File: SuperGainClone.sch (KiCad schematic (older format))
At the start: 99 parts, among them J1 Conn_01x02, J2 Conn_01x03, J3 Conn_01x02, J4 Conn_01x02, J5 Conn_01x02, Q1 TIP41C, Q2 TIP42C, U1 OPA2604A, U2 LM3886T, U3 OPA2604A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

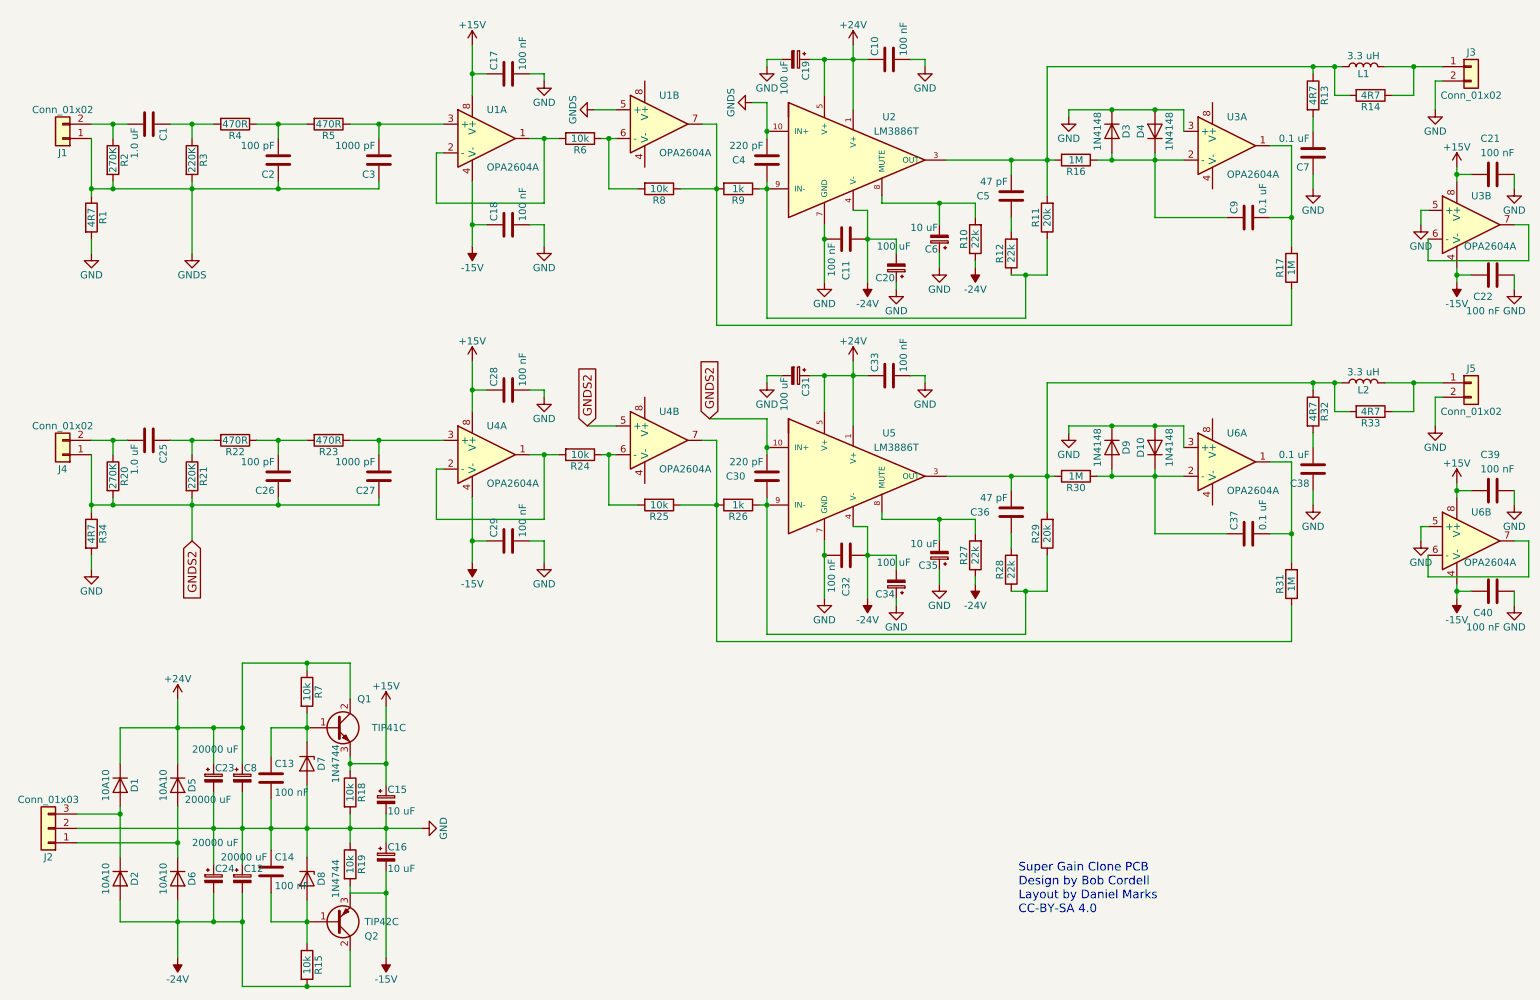
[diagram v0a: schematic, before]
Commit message: Rearranged some components
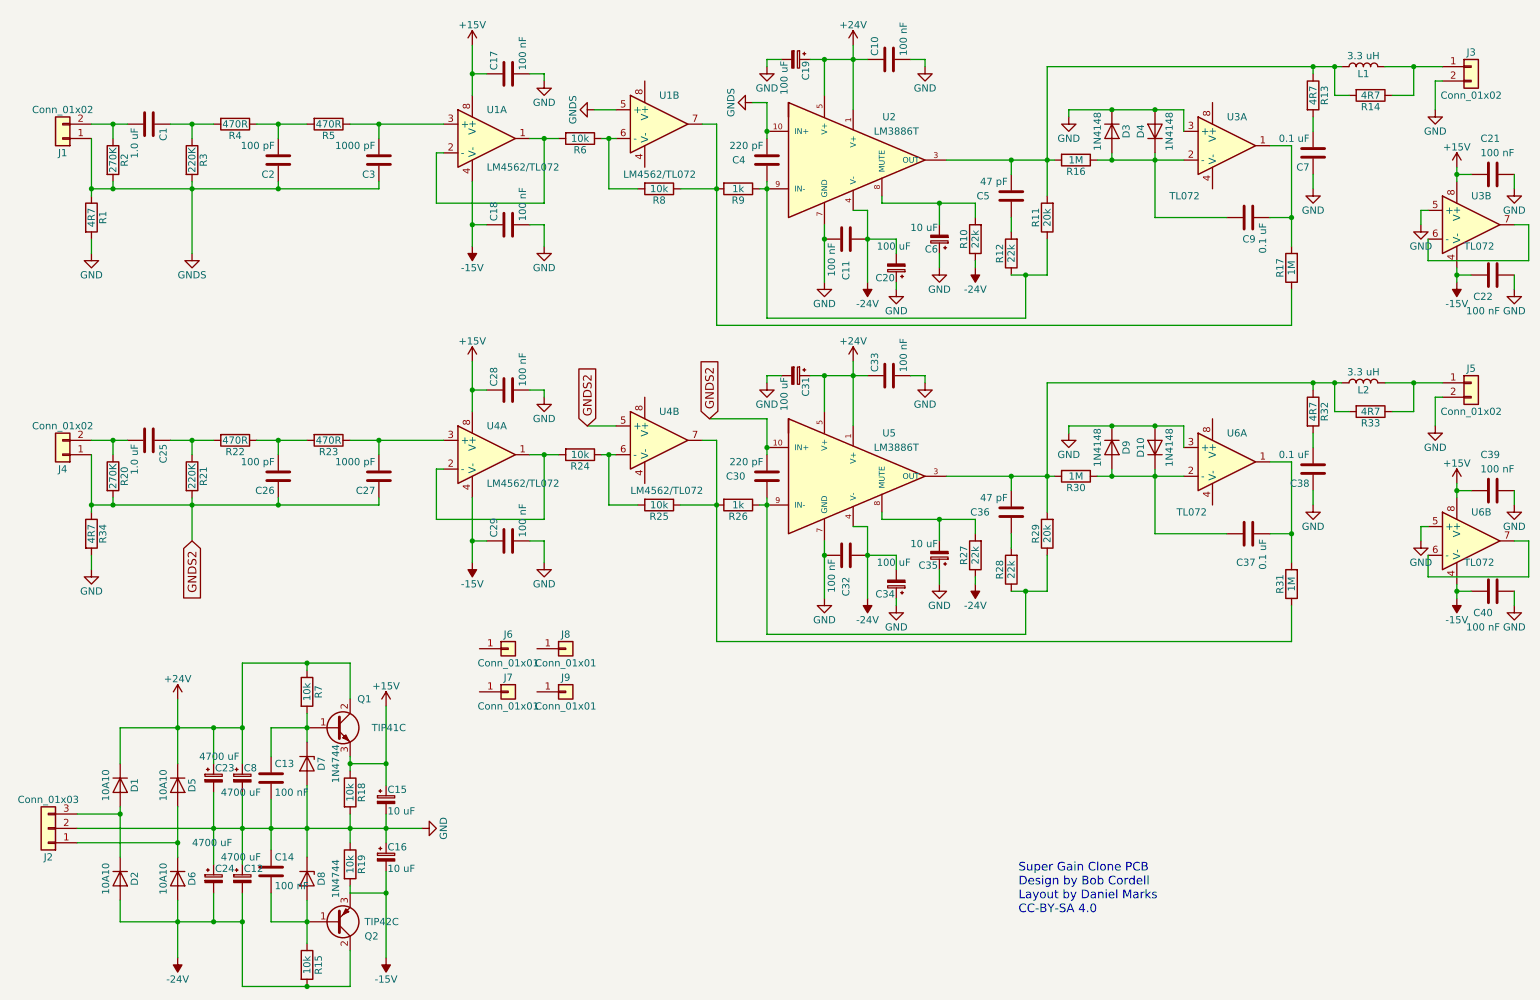
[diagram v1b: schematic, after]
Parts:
- added J6, J7, J8, J9: Conn_01x01, Connectors:1pin, symbol Conn_01x01
- C12, C23, C24, C8: value 20000 uF -> 4700 uF
- U1, U4: value OPA2604A -> LM4562/TL072
- U3, U6: value OPA2604A -> TL072

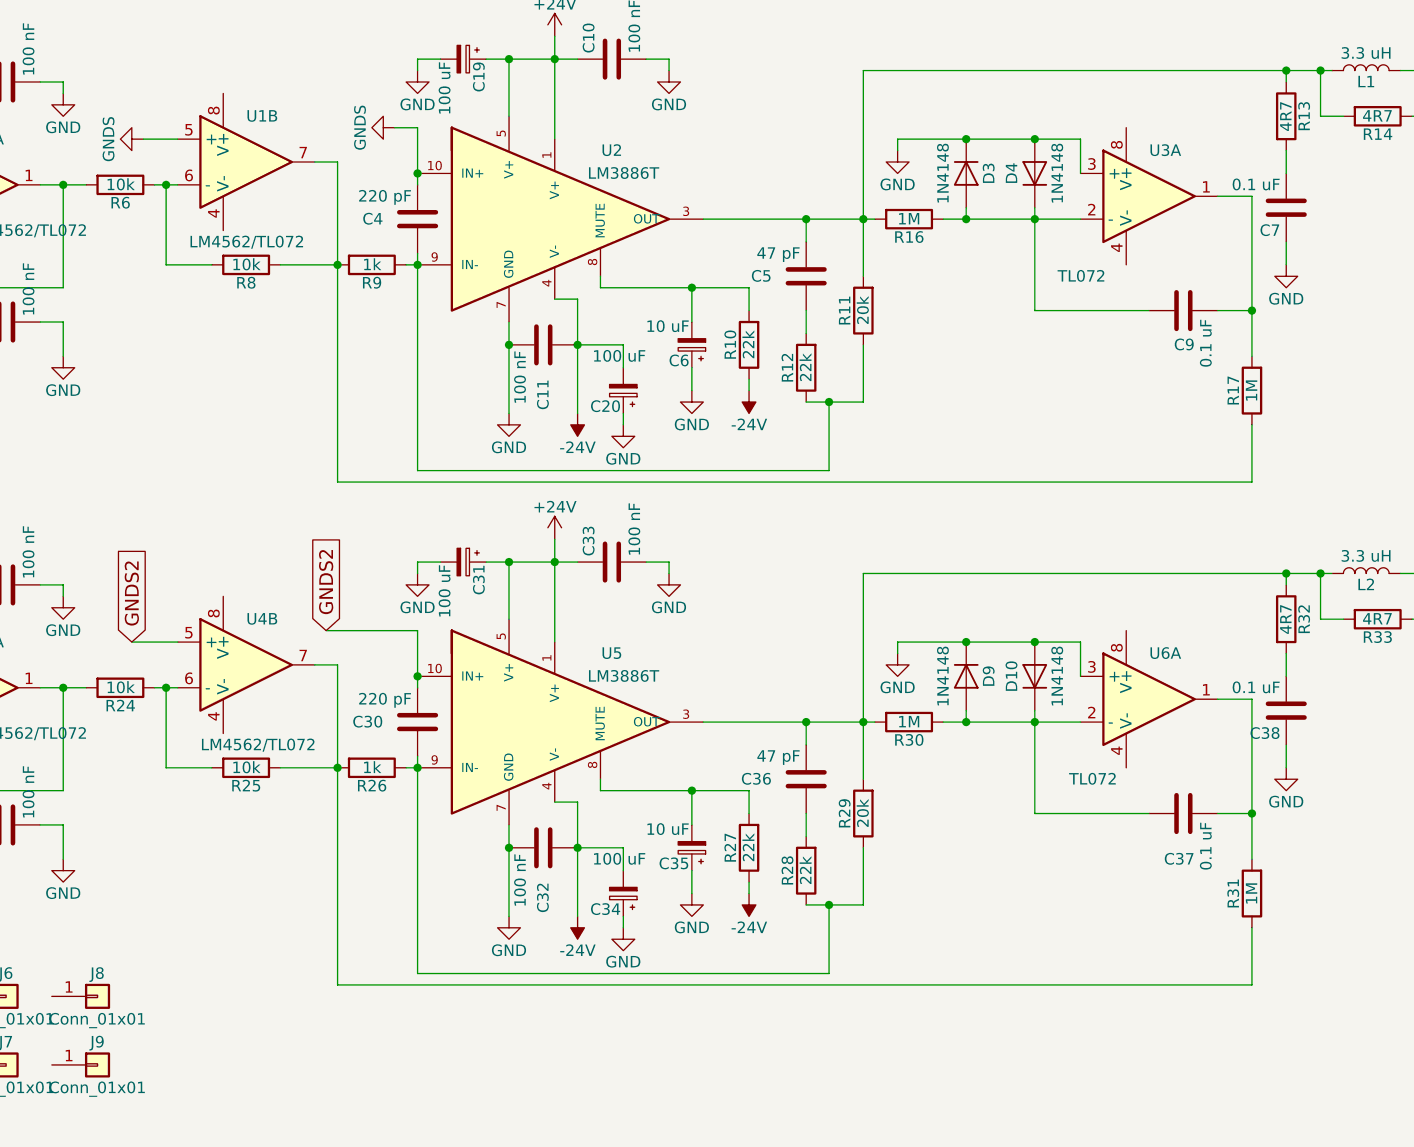
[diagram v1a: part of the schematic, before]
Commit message: Fixed DC servo feedback
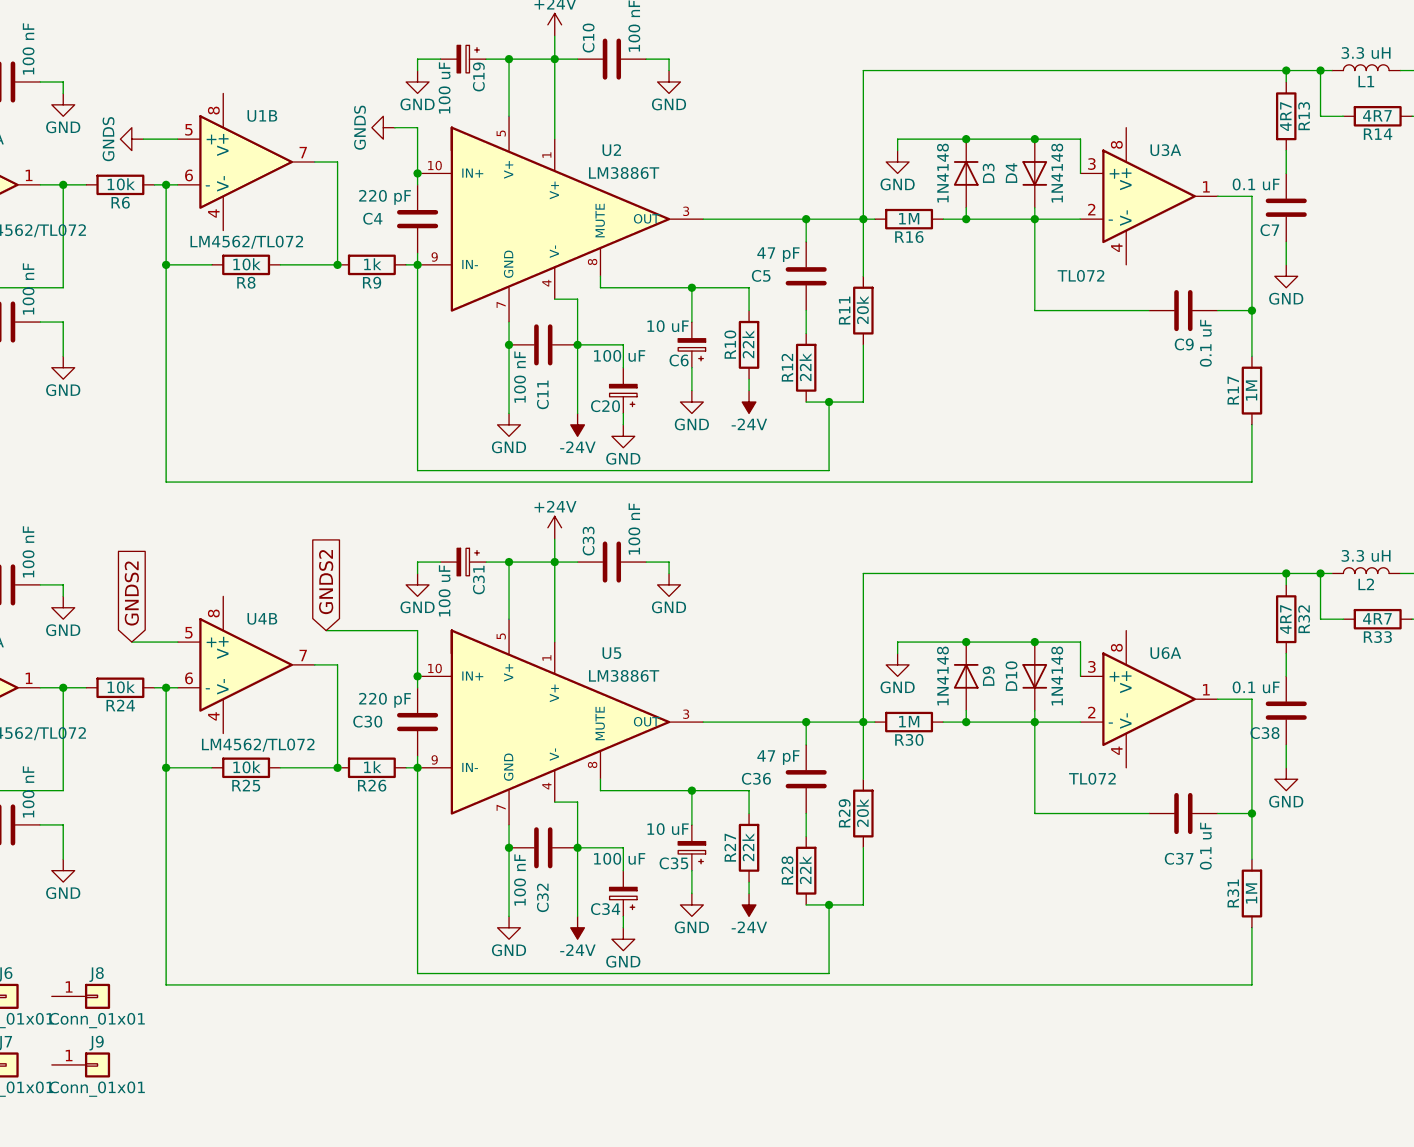
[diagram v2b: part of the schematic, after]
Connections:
- net at R6.1, R8.2, U1.6 (-): now also R17.1
- net at R8.1, R9.2, U1.7: no longer R17.1
- net at R24.1, R25.2, U4.6 (-): now also R31.1
- net at R25.1, R26.2, U4.7: no longer R31.1
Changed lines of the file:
@@
 	4550 1450 4700 1450
 Wire Wire Line
-	5400 1550 5400 2950
+	5400 1550 5400 2000
 Wire Wire Line
 	5300 1550 5400 1550
@@
 Connection ~ 9400 2200
 Wire Wire Line
-	9400 2700 9400 2950
+	9400 2950 9400 2700
 Connection ~ 5400 2000
 Wire Wire Line
 	5400 2000 5150 2000
 Wire Wire Line
-	4650 1650 4650 2000
+	4650 1650 4650 2950
 Wire Wire Line
 	4650 2000 4850 2000
@@
 	7550 2900 5750 2900
 Wire Wire Line
-	9400 2950 5400 2950
+	4650 2950 9400 2950
 $Comp
 L Conn_01x02 J4
@@
 	4500 3650 4700 3650
 Wire Wire Line
-	5400 3750 5400 5150
+	5400 3750 5400 4200
 Wire Wire Line
 	5300 3750 5400 3750
@@
 Connection ~ 9400 4400
 Wire Wire Line
-	9400 4900 9400 5150
+	9400 5150 9400 4900
 Connection ~ 5400 4200
 Wire Wire Line
 	5400 4200 5150 4200
 Wire Wire Line
-	4650 3850 4650 4200
+	4650 3850 4650 5150
 Wire Wire Line
 	4650 4200 4850 4200
@@
 	7550 5100 5750 5100
 Wire Wire Line
-	9400 5150 5400 5150
+	4650 5150 9400 5150
 $Comp
 L R R34
@@
 	1    0    0    -1
 $EndComp
+Connection ~ 4650 4200
+Connection ~ 4650 2000
 $EndSCHEMATC
